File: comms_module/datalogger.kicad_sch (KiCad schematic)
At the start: 56 parts, among them J1 Conn_Coaxial, J7 Conn_01x08_Socket, U1 BMP581, U2 DEVKIT_V1_ESP32-WROOM-32, U3 TPS79333-EP, U4 ICM-20948, U5 TPS79318-EP, U6 SN74AVC4T774RSVR, U7 ZEDFP9

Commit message: assigned footprints
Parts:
- C18: footprint (none) -> Capacitor_SMD:C_0402_1005Metric_Pad0.74x0.62mm_HandSolder
- FB4: footprint (none) -> Inductor_SMD:L_0402_1005Metric_Pad0.77x0.64mm_HandSolder
- J1: footprint (none) -> Connector_Coaxial:U.FL_Hirose_U.FL-R-SMT-1_Vertical
- JP1: footprint (none) -> Jumper:SolderJumper-2_P1.3mm_Open_Pad1.0x1.5mm
- JP2: footprint (none) -> Jumper:SolderJumper-2_P1.3mm_Bridged_Pad1.0x1.5mm
- R1, R12, R13, R14, R15, R16, R17, R18, R19, R2, R20, R3, R4, R5, R6: footprint (none) -> Resistor_SMD:R_0402_1005Metric_Pad0.72x0.64mm_HandSolder
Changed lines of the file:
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@@
 			)
 		)
-		(property "Footprint" ""
+		(property "Footprint" "Resistor_SMD:R_0402_1005Metric_Pad0.72x0.64mm_HandSolder"
 			(at 33.02 105.918 90)
 			(effects
@@
 			)
 		)
-		(property "Footprint" ""
+		(property "Footprint" "Resistor_SMD:R_0402_1005Metric_Pad0.72x0.64mm_HandSolder"
 			(at 91.44 112.268 90)
 			(effects
@@
 			)
 		)
-		(property "Footprint" ""
+		(property "Footprint" "Resistor_SMD:R_0402_1005Metric_Pad0.72x0.64mm_HandSolder"
 			(at 91.44 91.948 90)
 			(effects
@@
 			)
 		)
-		(property "Footprint" ""
+		(property "Footprint" "Resistor_SMD:R_0402_1005Metric_Pad0.72x0.64mm_HandSolder"
 			(at 91.44 109.728 90)
 			(effects
@@
 			)
 		)
-		(property "Footprint" ""
+		(property "Footprint" "Resistor_SMD:R_0402_1005Metric_Pad0.72x0.64mm_HandSolder"
 			(at 123.698 80.01 90)
 			(effects
@@
 			)
 		)
-		(property "Footprint" ""
+		(property "Footprint" "Resistor_SMD:R_0402_1005Metric_Pad0.72x0.64mm_HandSolder"
 			(at 91.44 121.158 90)
 			(effects
@@
 			)
 		)
-		(property "Footprint" ""
+		(property "Footprint" "Capacitor_SMD:C_0402_1005Metric_Pad0.74x0.62mm_HandSolder"
 			(at 25.0952 114.3 0)
 			(effects
@@
 			)
 		)
-		(property "Footprint" ""
+		(property "Footprint" "Jumper:SolderJumper-2_P1.3mm_Open_Pad1.0x1.5mm"
 			(at 121.92 109.22 0)
 			(effects
@@
 			)
 		)
-		(property "Footprint" ""
+		(property "Footprint" "Resistor_SMD:R_0402_1005Metric_Pad0.72x0.64mm_HandSolder"
 			(at 91.44 99.568 90)
 			(effects
@@
 			)
 		)
-		(property "Footprint" ""
+		(property "Footprint" "Inductor_SMD:L_0402_1005Metric_Pad0.77x0.64mm_HandSolder"
 			(at 22.352 99.06 90)
 			(effects
@@
 			)
 		)
-		(property "Footprint" ""
+		(property "Footprint" "Resistor_SMD:R_0402_1005Metric_Pad0.72x0.64mm_HandSolder"
 			(at 91.44 116.078 90)
 			(effects
@@
 			)
 		)
-		(property "Footprint" ""
+		(property "Footprint" "Resistor_SMD:R_0402_1005Metric_Pad0.72x0.64mm_HandSolder"
 			(at 91.44 102.108 90)
 			(effects
@@
 			)
 		)
-		(property "Footprint" ""
+		(property "Footprint" "Resistor_SMD:R_0402_1005Metric_Pad0.72x0.64mm_HandSolder"
 			(at 91.44 86.868 90)
 			(effects
@@
 			)
 		)
-		(property "Footprint" ""
+		(property "Footprint" "Resistor_SMD:R_0402_1005Metric_Pad0.72x0.64mm_HandSolder"
 			(at 91.44 124.968 90)
 			(effects
@@
 			)
 		)
-		(property "Footprint" ""
+		(property "Footprint" "Jumper:SolderJumper-2_P1.3mm_Bridged_Pad1.0x1.5mm"
 			(at 127 73.66 0)
 			(effects
@@
 			)
 		)
-		(property "Footprint" ""
+		(property "Footprint" "Resistor_SMD:R_0402_1005Metric_Pad0.72x0.64mm_HandSolder"
 			(at 133.858 80.01 90)
 			(effects
@@
 			)
 		)
-		(property "Footprint" ""
+		(property "Footprint" "Resistor_SMD:R_0402_1005Metric_Pad0.72x0.64mm_HandSolder"
 			(at 91.44 89.408 90)
 			(effects
@@
 			)
 		)
-		(property "Footprint" ""
+		(property "Footprint" "Resistor_SMD:R_0402_1005Metric_Pad0.72x0.64mm_HandSolder"
 			(at 91.44 84.328 90)
 			(effects
@@
 			)
 		)
-		(property "Footprint" ""
+		(property "Footprint" "Resistor_SMD:R_0402_1005Metric_Pad0.72x0.64mm_HandSolder"
 			(at 91.44 118.618 90)
 			(effects
@@
 			)
 		)
-		(property "Footprint" ""
+		(property "Footprint" "Connector_Coaxial:U.FL_Hirose_U.FL-R-SMT-1_Vertical"
 			(at 17.78 91.44 0)
 			(effects

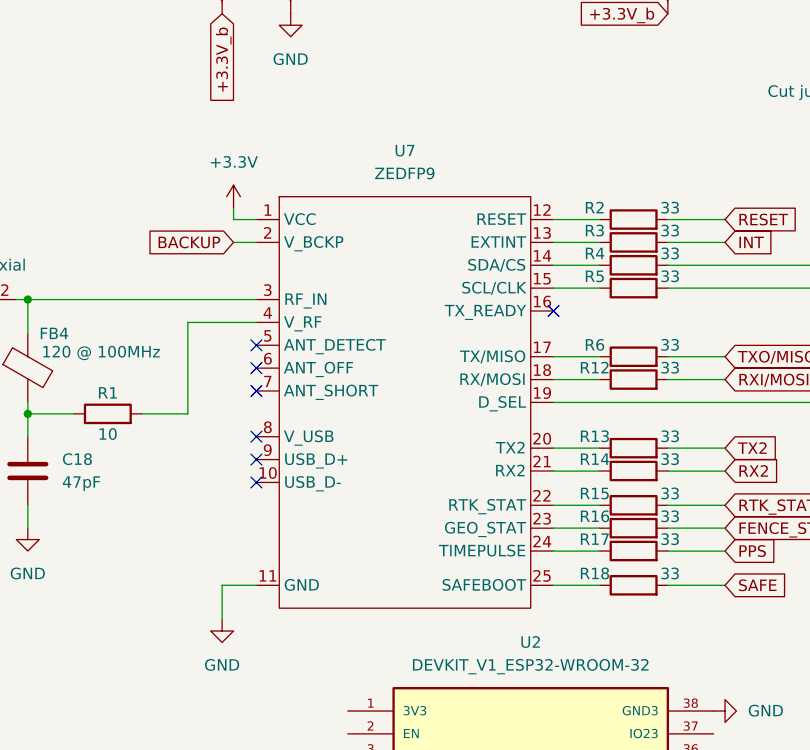
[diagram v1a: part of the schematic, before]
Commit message: assigned footprints
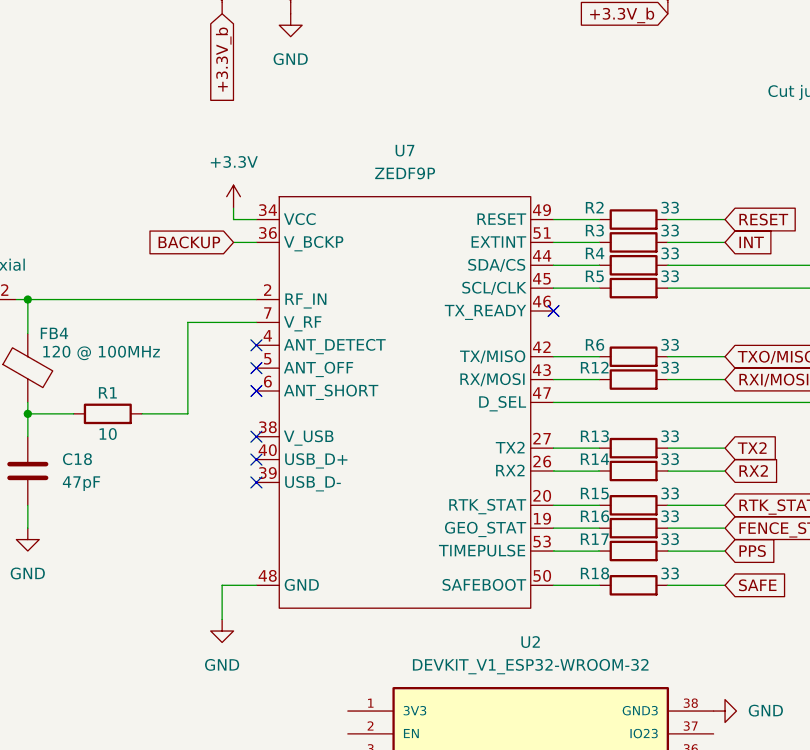
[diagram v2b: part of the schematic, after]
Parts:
- removed U7: ZEDFP9, symbol comms_module_stuff:ZEDFP9_module
- added U7: ZEDF9P, zedf9p:SMT_F9P-02B_UBL, symbol comms_module_stuff:ZEDF9P_module
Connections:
- net +3.3V: now also U7.34 (VCC)
- net BACKUP: now also U7.36 (V_BCKP)
- net GND: now also U7.48 (GND)
- net at R1.2: now also U7.7 (V_RF)
- net at R14.1: now also U7.26 (RX2)
- net at R5.1: now also U7.45 (SCL/CLK)
- net at R13.1: now also U7.27 (TX2)
- net at R2.1: now also U7.49 (RESET)
- net at R3.1: now also U7.51 (EXTINT)
- net at R4.1: now also U7.44 (SDA/CS)
- net at R6.1: now also U7.42 (TX/MISO)
- net at R12.1: now also U7.43 (RX/MOSI)
- net at JP1.2 (B): now also U7.47 (D_SEL)
- net at R15.1: now also U7.20 (RTK_STAT)
- net at R16.1: now also U7.19 (GEO_STAT)
- net at R17.1: now also U7.53 (TIMEPULSE)
- net at R18.1: now also U7.50 (SAFEBOOT)
- net at FB4.1, J1.2 (Ext): now also U7.2 (RF_IN)

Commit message: RF component schematic
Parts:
- added C19, C20, C21, C22, C23, C24, C25, C26, C27, C28, C29, C33, C34, C35: C, symbol Device:C
- added C30: 470nF, symbol Device:C
- added C31: 100nF, symbol Device:C
- added C32, C36: 1nF, symbol Device:C
- added J2: Conn_Coaxial, symbol Connector:Conn_Coaxial
- added L1, L2, L3, L4, L5, L7, L8: L, symbol Device:L
- added L6: 15uH, symbol Device:L
- added R21, R22: 100R, symbol Device:R
- added U8: SX1261IMLTRT, SX1261IMLTRT:QFN4x4_SEM, symbol SX1261IMLTRT:SX1261IMLTRT
- added U9: 4259-63, PE4259:SC-70-6_PSM, symbol PE4259:4259-63
- added Y2: Crystal 32MHz, KiCad:NX2016SA32MEXS00ACS06465, symbol Device:Crystal_GND24
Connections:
- net GND: now also C19.2, C20.2, C22.2, C23.2, C25.2, C27.2, C28.2, C29.2, C30.2, C31.2, C32.2, C34.2, C35.2, C36.2, J2.2 (Ext), U8.2 (GND), U8.20 (GND), U8.25 (GND), U8.5 (GND), U8.8 (GND), U9.2 (GND), Y2.2, Y2.4
- new net: C36.1, R22.2, U9.4 (CTRL)
- new net: C30.1, L6.1, L7.1, U8.7 (VREG)
- new net: L6.2, U8.9 (DCC_SW)
- new net: C35.1, J2.1 (In), L8.2
- new net: C26.1, L5.2, U8.22 (RFI_N)
- new net: C26.2, C27.1, U9.3 (RF2)
- new net: L2.1, U8.23 (RFO)
- new net: C21.1, C22.1, L1.2, L2.2, L3.1
- new net: C33.1, C34.1, L8.1
- new net: C21.2, C23.1, C24.1, L3.2
- new net: C24.2, L4.1
- new net: U8.4 (XTB), Y2.1
- new net: U8.3 (XTA), Y2.3
- new net: C29.1, L7.2, U8.1 (VDD_IN)
- new net: C28.1, L5.1, U8.21 (RFI_P)
- new net: C19.1, C20.1, L1.1, U8.24 (VR_PA)
- new net: C25.1, L4.2, U9.1 (RF1)
- new net: C32.1, R21.2, U9.6 (*CTRL/VDD)
- new net: C33.2, U9.5 (RFC)
- new net ANT SW: R21.1
- new net BUSY: U8.14 (BUSY)
- new net DIO1: U8.13 (DIO1)
- new net DIO2: R22.1, U8.12 (DIO2)
- new net DIO3: U8.6 (DIO3)
- new net MISO: U8.16 (MISO)
- new net MOSI: U8.17 (MOSI)
- new net NSS: U8.19 (NSS)
- new net SCK: U8.18 (SCK)
- new net SX_NRESET: U8.15 (NRESET)
- new net VDD RADIO: C31.1, U8.10 (VBAT), U8.11 (VBAT_IO)
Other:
- moved on the sheet: C1, C10, C11, C12, C13, C14, C15, C16, C17, C18, C4, C5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
